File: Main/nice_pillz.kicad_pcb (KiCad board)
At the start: 2 copper layers, 100 x 86 mm, 28 parts, among them J1 Conn_01x13, J2 Conn_01x13, J3 Conn_01x13, J4 Conn_01x13, J5 Conn_01x10, J6 Conn_01x10, J7 Conn_01x13, J8 Conn_01x13, M1 MountingHole_6.4mm_M6, M3 MountingHole_4.3mm_M4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

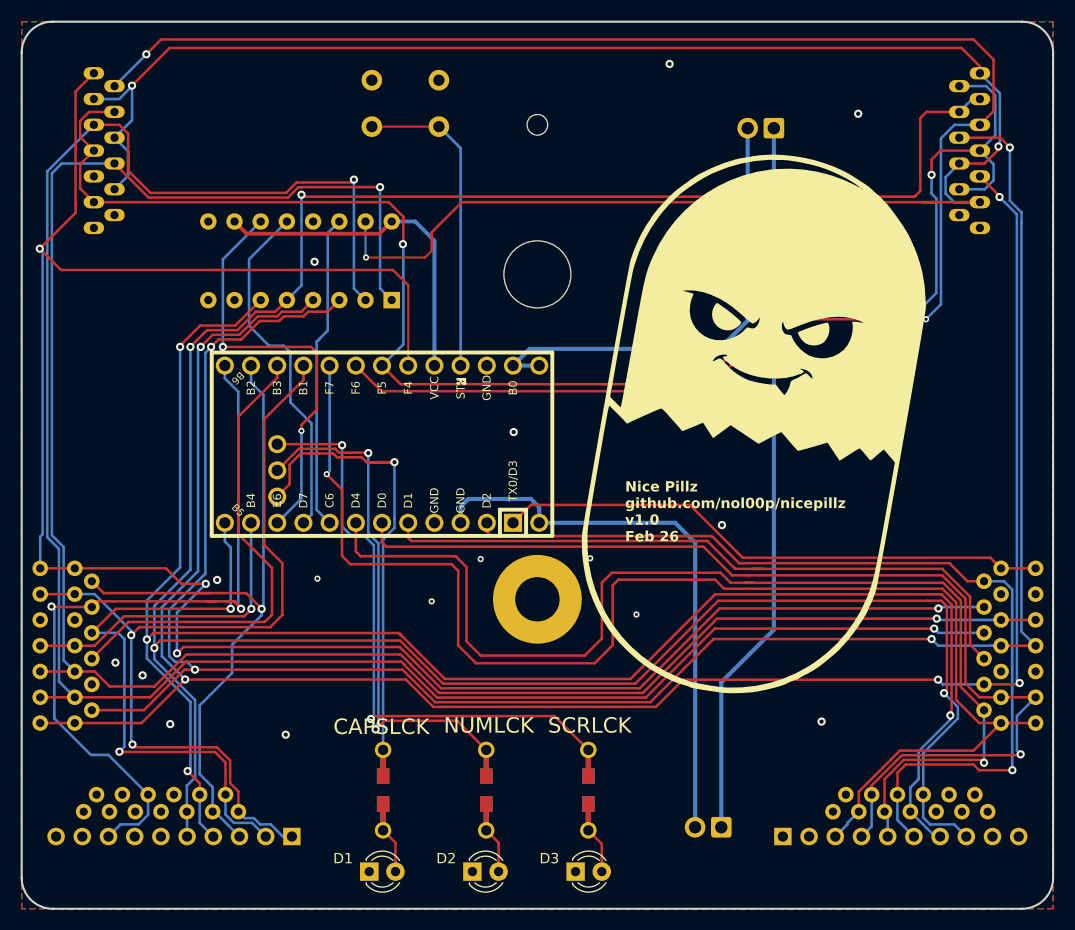
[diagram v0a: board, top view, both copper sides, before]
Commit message: v1.1 new pcb and overlay config
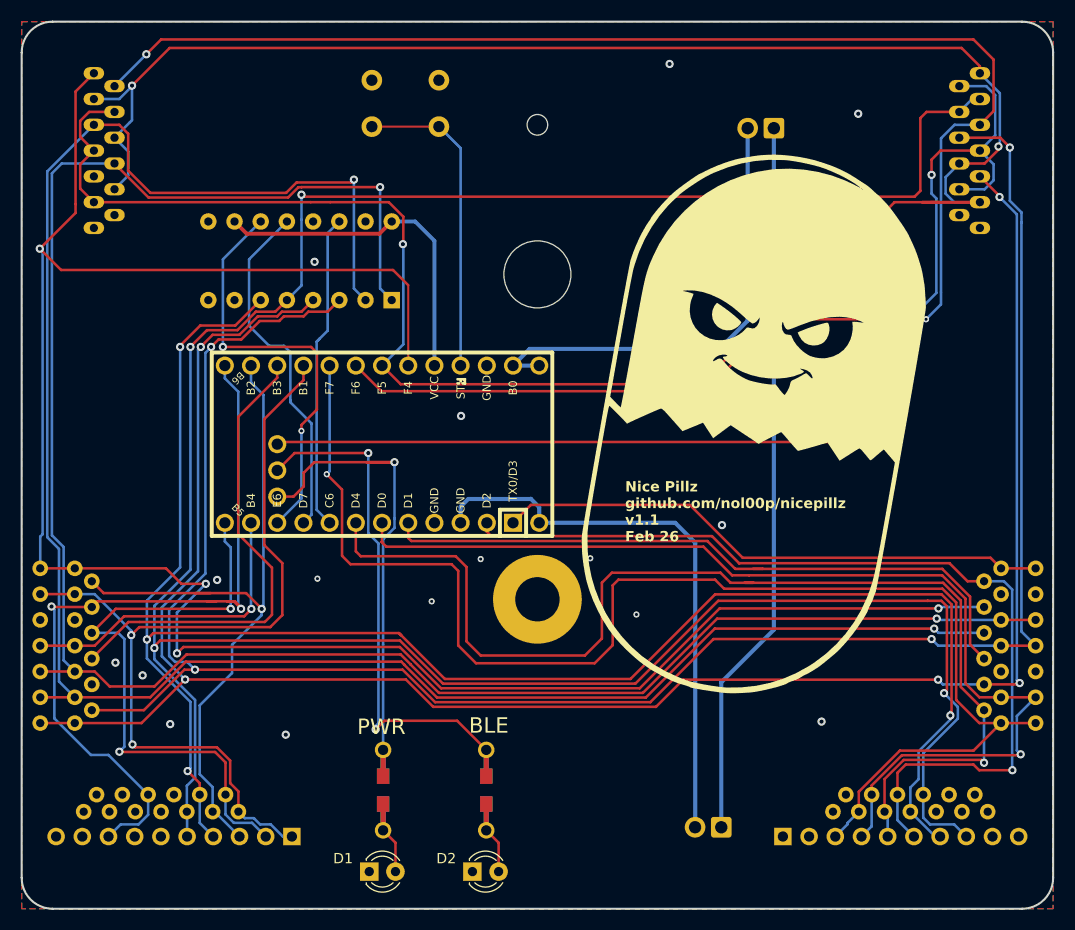
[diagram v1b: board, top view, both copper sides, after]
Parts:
- removed D3: LED_SCR, LED_THT:LED_D3.0mm
- removed R3: R_US, Keebio-Parts:Resistor-Hybrid
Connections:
- U1 pad 28: /LED_SCROLL_LOCK -> /ROW_13
- U2 pad 15: /ROW_13 -> (no net)
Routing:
- net /LED_SCROLL_LOCK: track 57.5 -> 0.00 mm, vias 2 -> 0
- net /ROW_13: track 189.8 -> 218.8 mm, vias 3 -> 4
- net Net-(D3-A): track 4.54 -> 0.00 mm
- net /LED_CAPS_LOCK: track 45.7 -> 47.4 mm
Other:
- board text added: "BLE"
- board text added: "Nice Pillz github.com/nol00p/nicepillz v1.1 Feb 26"
- board text added: "PWR"
- board text removed: "CAPSLCK"
- board text removed: "NUMLCK"
- board text removed: "Nice Pillz github.com/nol00p/nicepillz v1.0 Feb 26"
- board text removed: "SCRLCK"
